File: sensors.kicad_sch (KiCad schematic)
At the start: 43 parts

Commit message: updated pcb
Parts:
- removed ANT1: RF Antenna, 5449692-1:TE_5449692-1, symbol 5449692-1:5449692-1
- added ANT1: 5-1814832-1, 5-1814832-1:TE_5-1814832-1, symbol 5-1814832-1:5-1814832-1
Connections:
- net GND: now also ANT1.2, ANT1.3 (2), ANT1.4 (2), ANT1.5 (2)
- net RFM95W_ANT: now also ANT1.1
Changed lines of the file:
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@@
     (stroke (width 0) (type default))
   )
-  (wire (pts (xy 264.16 137.16) (xy 260.35 137.16))
+  (wire (pts (xy 264.16 138.43) (xy 260.35 138.43))
     (stroke (width 0) (type default))
   )
@@
     )
   )
-  (symbol (lib_id "power:GND") (at 264.16 137.16 90) (unit 1)
-    (in_bom yes) (on_board yes) (dnp no) (fields_autoplaced)
-    (property "Reference" "#PWR?" (at 270.51 137.16 0)
-      (effects (font (size 1.27 1.27)) hide)
-    )
-    (property "Value" "GND" (at 267.97 137.16 90)
-      (effects (font (size 1.27 1.27)) (justify right) hide)
-    )
-    (property "Footprint" "" (at 264.16 137.16 0)
-      (effects (font (size 1.27 1.27)) hide)
-    )
-    (property "Datasheet" "" (at 264.16 137.16 0)
+  (symbol (lib_id "power:GND") (at 264.16 138.43 90) (unit 1)
+    (in_bom yes) (on_board yes) (dnp no) (fields_autoplaced)
+    (property "Reference" "#PWR?" (at 270.51 138.43 0)
+      (effects (font (size 1.27 1.27)) hide)
+    )
+    (property "Value" "GND" (at 267.97 138.43 90)
+      (effects (font (size 1.27 1.27)) (justify right) hide)
+    )
+    (property "Footprint" "" (at 264.16 138.43 0)
+      (effects (font (size 1.27 1.27)) hide)
+    )
+    (property "Datasheet" "" (at 264.16 138.43 0)
       (effects (font (size 1.27 1.27)) hide)
     )
@@
         (path "/e12346fa-509d-4de9-8ab1-dced307292db/b5ec7ecd-943d-4169-981a-c46b6432f873"
           (reference "R30") (unit 1)
-        )
-      )
-    )
-  )
-  (symbol (lib_id "5449692-1:5449692-1") (at 257.81 137.16 0) (unit 1)
-    (in_bom yes) (on_board yes) (dnp no) (fields_autoplaced)
-    (property "Reference" "ANT1" (at 257.429 127 0)
-      (effects (font (size 1.27 1.27)))
-    )
-    (property "Value" "RF Antenna" (at 257.429 129.54 0)
-      (effects (font (size 1.27 1.27)))
-    )
-    (property "Footprint" "5449692-1:TE_5449692-1" (at 257.81 142.24 0)
-      (effects (font (size 1.27 1.27)) (justify bottom) hide)
-    )
-    (property "Datasheet" "" (at 257.81 137.16 0)
-      (effects (font (size 1.27 1.27)) hide)
-    )
-    (property "Comment" "5449692-1" (at 257.81 140.97 0)
-      (effects (font (size 1.27 1.27)) (justify bottom) hide)
-    )
-    (pin "1")
-    (pin "GND")
-    (pin "GND")
-    (instances
-      (project "aether"
-        (path "/e12346fa-509d-4de9-8ab1-dced307292db/b5ec7ecd-943d-4169-981a-c46b6432f873"
-          (reference "ANT1") (unit 1)
         )
       )
@@
         )
       )
+    )
+  )
+  (symbol (lib_id "5-1814832-1:5-1814832-1") (at 257.81 135.89 0) (unit 1)
+    (in_bom yes) (on_board yes) (dnp no) (fields_autoplaced)
+    (property "Reference" "ANT1" (at 256.667 127 0)
+      (effects (font (size 1.27 1.27)))
+    )
+    (property "Value" "5-1814832-1" (at 256.667 129.54 0)
+      (effects (font (size 1.27 1.27)))
+    )
+    (property "Footprint" "5-1814832-1:TE_5-1814832-1" (at 257.81 135.89 0)
+      (effects (font (size 1.27 1.27)) (justify bottom) hide)
+    )
+    (property "Datasheet" "" (at 257.81 135.89 0)
+      (effects (font (size 1.27 1.27)) hide)
+    )
+    (property "Comment" "5-1814832-1" (at 257.81 135.89 0)
+      (effects (font (size 1.27 1.27)) (justify bottom) hide)
+    )
+    (property "MF" "TE Connectivity" (at 257.81 135.89 0)
+      (effects (font (size 1.27 1.27)) (justify bottom) hide)
+    )
+    (property "Description" "\nConnector SMA JACK STR 50 OHM PCB | TE Connectivity 5-1814832-1\n" (at 257.81 135.89 0)
+      (effects (font (size 1.27 1.27)) (justify bottom) hide)
+    )
+    (property "Package" "None" (at 257.81 135.89 0)
+      (effects (font (size 1.27 1.27)) (justify bottom) hide)
+    )
+    (property "Price" "None" (at 257.81 135.89 0)
+      (effects (font (size 1.27 1.27)) (justify bottom) hide)
+    )
+    (property "Check_prices" "https://www.snapeda.com/parts/5-1814832-1/TE+Connectivity+AMP+Connectors/view-part/?ref=eda" (at 257.81 135.89 0)
+      (effects (font (size 1.27 1.27)) (justify bottom) hide)
+    )
+    (property "STANDARD" "Manufacturer recommendations" (at 257.81 135.89 0)
+      (effects (font (size 1.27 1.27)) (justify bottom) hide)
+    )
+    (property "PARTREV" "B1" (at 257.81 135.89 0)
+      (effects (font (size 1.27 1.27)) (justify bottom) hide)
+    )
+    (property "SnapEDA_Link" "https://www.snapeda.com/parts/5-1814832-1/TE+Connectivity+AMP+Connectors/view-part/?ref=snap" (at 257.81 135.89 0)
+      (effects (font (size 1.27 1.27)) (justify bottom) hide)
+    )
+    (property "MP" "5-1814832-1" (at 257.81 135.89 0)
+      (effects (font (size 1.27 1.27)) (justify bottom) hide)
+    )
+    (property "Purchase-URL" "https://www.snapeda.com/api/url_track_click_mouser/?unipart_id=38815&manufacturer=TE Connectivity&part_name=5-1814832-1&search_term=5-1814832-1" (at 257.81 135.89 0)
+      (effects (font (size 1.27 1.27)) (justify bottom) hide)
+    )
+    (property "EU_RoHS_Compliance" "Compliant with Exemptions" (at 257.81 135.89 0)
+      (effects (font (size 1.27 1.27)) (justify bottom) hide)
+    )
+    (property "Number_of_Positions" "1" (at 257.81 135.89 0)
+      (effects (font (size 1.27 1.27)) (justify bottom) hide)
+    )
+    (property "Availability" "In Stock" (at 257.81 135.89 0)
+      (effects (font (size 1.27 1.27)) (justify bottom) hide)
+    )
+    (property "MANUFACTURER" "TE Connectivity" (at 257.81 135.89 0)
+      (effects (font (size 1.27 1.27)) (justify bottom) hide)
+    )
+    (pin "1")
+    (pin "2")
+    (pin "3")
+    (pin "4")
+    (pin "5")
+    (instances
+      (project "aether"
+        (path "/e12346fa-509d-4de9-8ab1-dced307292db/b5ec7ecd-943d-4169-981a-c46b6432f873"
+          (reference "ANT1") (unit 1)
+        )
+      )

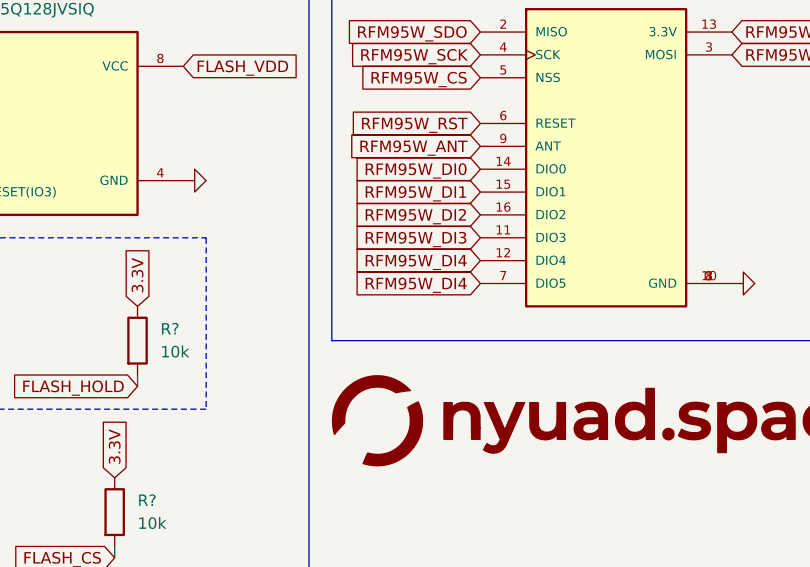
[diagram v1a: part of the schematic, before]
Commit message: updated tracks
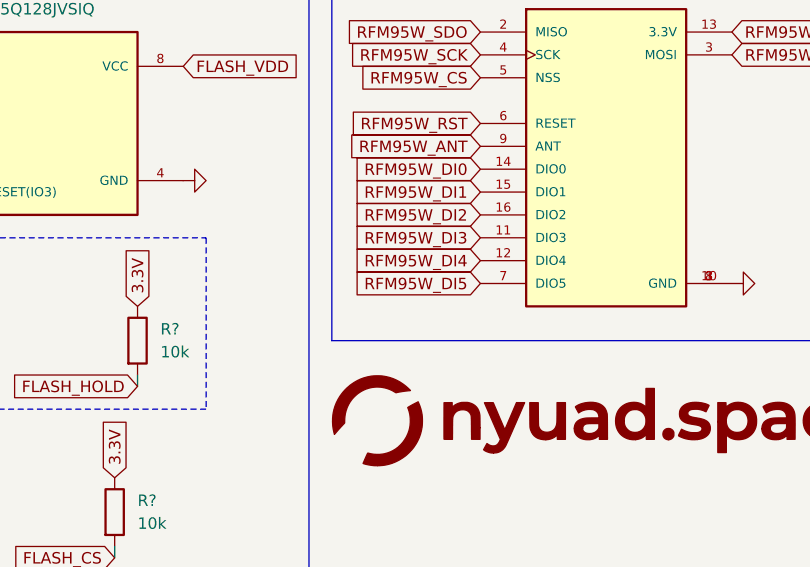
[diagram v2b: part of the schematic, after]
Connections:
- net RFM95W_DI4: no longer U?.7 (DIO5)
- new net RFM95W_DI5: U?.7 (DIO5)
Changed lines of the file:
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@@
     )
   )
-  (global_label "RFM95W_DI4" (shape input) (at 194.31 157.48 180) (fields_autoplaced)
+  (global_label "RFM95W_DI5" (shape input) (at 194.31 157.48 180) (fields_autoplaced)
     (effects (font (size 1.27 1.27)) (justify right))
     (property "Intersheetrefs" "${INTERSHEET_REFS}" (at 179.5925 157.48 0)

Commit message: started routing
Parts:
- R? (x4): footprint Resistor_SMD:R_0603_1608Metric -> Resistor_SMD:R_0402_1005Metric
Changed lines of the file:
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@@
       (effects (font (size 1.27 1.27)) (justify left))
     )
-    (property "Footprint" "Resistor_SMD:R_0603_1608Metric" (at 125.222 104.14 90)
+    (property "Footprint" "Resistor_SMD:R_0402_1005Metric" (at 125.222 104.14 90)
       (effects (font (size 1.27 1.27)) hide)
     )
@@
       (effects (font (size 1.27 1.27)) (justify left))
     )
-    (property "Footprint" "Resistor_SMD:R_0603_1608Metric" (at 250.952 156.21 90)
+    (property "Footprint" "Resistor_SMD:R_0402_1005Metric" (at 250.952 156.21 90)
       (effects (font (size 1.27 1.27)) hide)
     )
@@
       (effects (font (size 1.27 1.27)) (justify left))
     )
-    (property "Footprint" "Resistor_SMD:R_0603_1608Metric" (at 31.242 102.87 90)
+    (property "Footprint" "Resistor_SMD:R_0402_1005Metric" (at 31.242 102.87 90)
       (effects (font (size 1.27 1.27)) hide)
     )
@@
       (effects (font (size 1.27 1.27)) (justify left))
     )
-    (property "Footprint" "Resistor_SMD:R_0603_1608Metric" (at 93.472 172.72 90)
-      (effects (font (size 1.27 1.27)) hide)
-    )
+    (property "Footprint" "Resistor_SMD:R_0402_1005Metric" (at 93.472 172.72 90)
+      (effects (font (size 1.27 1.27)) hide)
+    )

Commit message: more routing
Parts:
- removed U?: PCA9685BS, Package_DFN_QFN:QFN-28-1EP_6x6mm_P0.65mm_EP4.25x4.25mm, symbol Driver_LED:PCA9685BS
- added U7: PCA9685PW, Package_SO:TSSOP-28_4.4x9.7mm_P0.65mm, symbol Driver_LED:PCA9685PW
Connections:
- net 3.3V: now also U7.28 (VDD)
- net GND: now also U7.14 (VSS), U7.2 (A1), U7.24 (A5), U7.25 (EXTCLK), U7.3 (A2), U7.4 (A3), U7.5 (A4)
- net PCA9685_SCL: now also U7.26 (SCL)
- net PWM0: now also U7.6 (LED0)
- net PWM1: now also U7.7 (LED1)
- net PWM2: now also U7.8 (LED2)
- net PWM3: now also U7.9 (LED3)
- net PWM4: now also U7.10 (LED4)
- net PWM5: now also U7.11 (LED5)
- net PWM6: now also U7.12 (LED6)
- net PWM7: now also U7.13 (LED7)
- net at R?.1: now also U7.1 (A0)
- net at R?.1: now also U7.23 (~{OE})
- new net: U7.15 (LED8), U7.16 (LED9), U7.17 (LED10), U7.18 (LED11), U7.19 (LED12), U7.20 (LED13), U7.21 (LED14), U7.22 (LED15)
- new net PCA9685_SDA: U7.27 (SDA)
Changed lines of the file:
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@@
   (junction (at 33.02 166.37) (diameter 0) (color 0 0 0 0)
   )
+  (junction (at 160.02 40.64) (diameter 0) (color 0 0 0 0)
+  )
+  (junction (at 160.02 48.26) (diameter 0) (color 0 0 0 0)
+  )
   (junction (at 218.44 53.34) (diameter 0) (color 0 0 0 0)
   )
@@
   (junction (at 133.35 181.61) (diameter 0) (color 0 0 0 0)
   )
-  (junction (at 160.02 40.64) (diameter 0) (color 0 0 0 0)
-  )
   (no_connect (at 218.44 35.56))
   (no_connect (at 195.58 52.07))
@@
     (stroke (width 0) (type default))
   )
+  (wire (pts (xy 158.75 29.21) (xy 160.02 29.21))
+    (stroke (width 0) (type default))
+  )
   (wire (pts (xy 149.86 54.61) (xy 152.4 54.61))
     (stroke (width 0) (type default))
@@
     (stroke (width 0) (type default))
   )
+  (wire (pts (xy 158.75 26.67) (xy 160.02 26.67))
+    (stroke (width 0) (type default))
+  )
   (wire (pts (xy 133.35 181.61) (xy 133.35 182.88))
     (stroke (width 0) (type default))
@@
     )
   )
-  (global_label "PCA9685_SCD" (shape input) (at 160.02 29.21 180) (fields_autoplaced)
+  (global_label "PCA9685_SDA" (shape input) (at 158.75 29.21 180) (fields_autoplaced)
     (effects (font (size 1.27 1.27)) (justify right))
-    (property "Intersheetrefs" "${INTERSHEET_REFS}" (at 143.8511 29.21 0)
+    (property "Intersheetrefs" "${INTERSHEET_REFS}" (at 142.7625 29.21 0)
       (effects (font (size 1.27 1.27)) (justify right) hide)
     )
@@
     )
   )
-  (global_label "PCA9685_SCL" (shape input) (at 160.02 26.67 180) (fields_autoplaced)
+  (global_label "PCA9685_SCL" (shape input) (at 158.75 26.67 180) (fields_autoplaced)
     (effects (font (size 1.27 1.27)) (justify right))
-    (property "Intersheetrefs" "${INTERSHEET_REFS}" (at 144.093 26.67 0)
+    (property "Intersheetrefs" "${INTERSHEET_REFS}" (at 142.823 26.67 0)
       (effects (font (size 1.27 1.27)) (justify right) hide)
     )
@@
     )
   )
+  (symbol (lib_id "Driver_LED:PCA9685PW") (at 177.8 44.45 0) (unit 1)
+    (in_bom yes) (on_board yes) (dnp no) (fields_autoplaced)
+    (property "Reference" "U7" (at 177.8 19.05 0)
+      (effects (font (size 1.27 1.27)))
+    )
+    (property "Value" "PCA9685PW" (at 177.8 21.59 0)
+      (effects (font (size 1.27 1.27)))
+    )
+    (property "Footprint" "Package_SO:TSSOP-28_4.4x9.7mm_P0.65mm" (at 178.435 69.215 0)
+      (effects (font (size 1.27 1.27)) (justify left) hide)
+    )
+    (property "Datasheet" "http://www.nxp.com/docs/en/data-sheet/PCA9685.pdf" (at 167.64 26.67 0)
+      (effects (font (size 1.27 1.27)) hide)
+    )
+    (pin "1")
+    (pin "10")
+    (pin "11")
+    (pin "12")
+    (pin "13")
+    (pin "14")
+    (pin "15")
+    (pin "16")
+    (pin "17")
+    (pin "18")
+    (pin "19")
+    (pin "2")
+    (pin "20")
+    (pin "21")
+    (pin "22")
+    (pin "23")
+    (pin "24")
+    (pin "25")
+    (pin "26")
+    (pin "27")
+    (pin "28")
+    (pin "3")
+    (pin "4")
+    (pin "5")
+    (pin "6")
+    (pin "7")
+    (pin "8")
+    (pin "9")
+    (instances
+      (project "aether"
+        (path "/e12346fa-509d-4de9-8ab1-dced307292db/b5ec7ecd-943d-4169-981a-c46b6432f873"
+          (reference "U7") (unit 1)
+        )
+      )
+    )
+  )
   (symbol (lib_id "power:GND") (at 218.44 55.88 0) (unit 1)
     (in_bom yes) (on_board yes) (dnp no) (fields_autoplaced)
@@
         )
       )
-    )
-  )
-  (symbol (lib_id "Driver_LED:PCA9685BS") (at 177.8 44.45 0) (unit 1)
-    (in_bom yes) (on_board yes) (dnp no)
-    (property "Reference" "U?" (at 175.26 20.32 0)
-      (effects (font (size 1.27 1.27)) (justify left))
-    )
-    (property "Value" "PCA9685BS" (at 172.72 22.86 0)
-      (effects (font (size 1.27 1.27)) (justify left))
-    )
-    (property "Footprint" "Package_DFN_QFN:QFN-28-1EP_6x6mm_P0.65mm_EP4.25x4.25mm" (at 178.435 69.215 0)
-      (effects (font (size 1.27 1.27)) (justify left) hide)
-    )
-    (property "Datasheet" "http://www.nxp.com/docs/en/data-sheet/PCA9685.pdf" (at 167.64 26.67 0)
-      (effects (font (size 1.27 1.27)) hide)
-    )
-    (pin "1")
-    (pin "10")
-    (pin "11")
-    (pin "12")
-    (pin "13")
-    (pin "14")
-    (pin "15")
-    (pin "16")
-    (pin "17")
-    (pin "18")
-    (pin "19")
-    (pin "2")
-    (pin "20")
-    (pin "21")
-    (pin "22")
-    (pin "23")
-    (pin "24")
-    (pin "25")
-    (pin "26")
-    (pin "27")
-    (pin "28")
-    (pin "29")
-    (pin "3")
-    (pin "4")
-    (pin "5")
-    (pin "6")
-    (pin "7")
-    (pin "8")
-    (pin "9")
-    (instances
-      (project "aether"
-        (path "/e12346fa-509d-4de9-8ab1-dced307292db"
-          (reference "U?") (unit 1)
-        )
-        (path "/e12346fa-509d-4de9-8ab1-dced307292db/b5ec7ecd-943d-4169-981a-c46b6432f873"
-          (reference "U7") (unit 1)
-        )
-      )

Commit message: significant amount of routing done
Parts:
- C?: footprint Capacitor_SMD:C_0603_1608Metric -> Capacitor_SMD:C_0402_1005Metric
- D?: footprint LED_SMD:LED_0603_1608Metric -> LED_SMD:LED_0402_1005Metric
- R? (x6): footprint Resistor_SMD:R_0603_1608Metric -> Resistor_SMD:R_0402_1005Metric
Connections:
- net PWM0: now also U7.13 (LED7); no longer U7.6 (LED0)
- net PWM1: now also U7.12 (LED6); no longer U7.7 (LED1)
- net PWM2: now also U7.11 (LED5); no longer U7.8 (LED2)
- net PWM3: now also U7.10 (LED4); no longer U7.9 (LED3)
- net PWM4: now also U7.9 (LED3); no longer U7.10 (LED4)
- net PWM5: now also U7.8 (LED2); no longer U7.11 (LED5)
- net PWM6: now also U7.7 (LED1); no longer U7.12 (LED6)
- net PWM7: now also U7.6 (LED0); no longer U7.13 (LED7)

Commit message: added power planes
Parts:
- R? (x2): footprint Resistor_SMD:R_0402_1005Metric -> Resistor_SMD:R_0603_1608Metric
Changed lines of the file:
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@@
       (effects (font (size 1.27 1.27)))
     )
-    (property "Footprint" "Resistor_SMD:R_0402_1005Metric" (at 60.96 52.578 90)
+    (property "Footprint" "Resistor_SMD:R_0603_1608Metric" (at 60.96 52.578 90)
       (effects (font (size 1.27 1.27)) hide)
     )
@@
       (effects (font (size 1.27 1.27)))
     )
-    (property "Footprint" "Resistor_SMD:R_0402_1005Metric" (at 60.96 46.482 90)
-      (effects (font (size 1.27 1.27)) hide)
-    )
+    (property "Footprint" "Resistor_SMD:R_0603_1608Metric" (at 60.96 46.482 90)
+      (effects (font (size 1.27 1.27)) hide)
+    )
